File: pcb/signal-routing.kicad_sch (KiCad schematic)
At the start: 42 parts, among them U10 SN74LVC1G3157DCKR, U11 SN74HCS595PWR, U3 SN74LVC1G3157DCKR, U4 SN74LVC1G3157DCKR, U5 SN74LVC1G3157DCKR, U6 SN74LVC1G3157DCKR, U7 SN74LVC1G3157DCKR, U8 SN74LVC1G3157DCKR, U9 SN74LVC1G3157DCKR

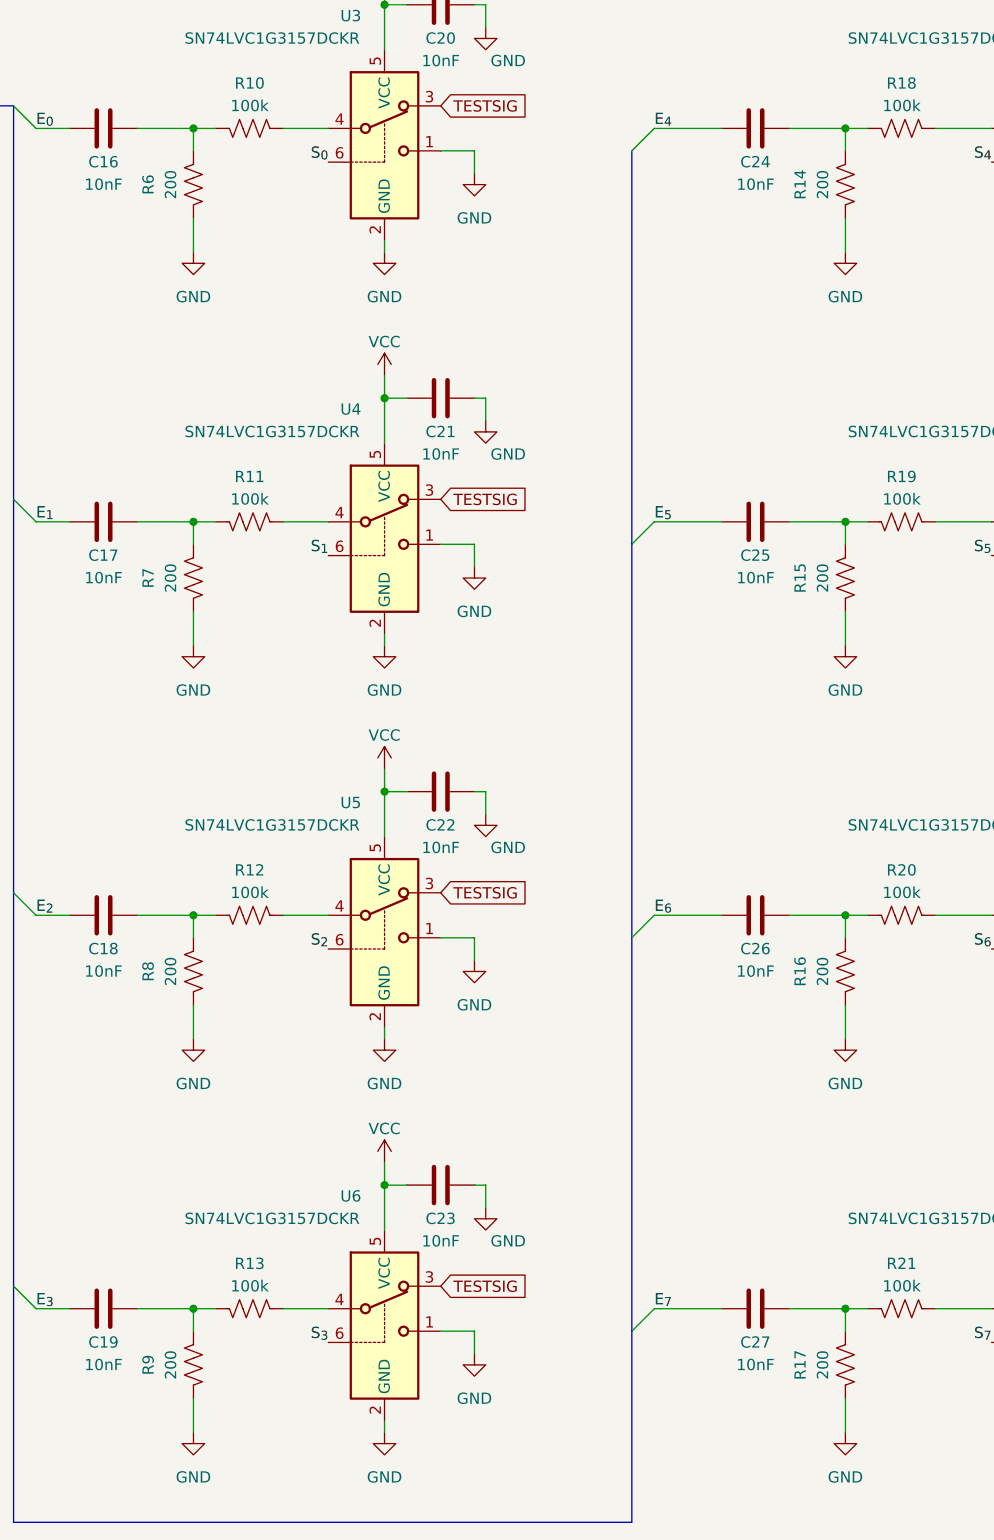
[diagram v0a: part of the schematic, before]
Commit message: Added OEPS PN.
Co-Authored-By: David Palma <78764277+davidpalma666@users.noreply.github.com>
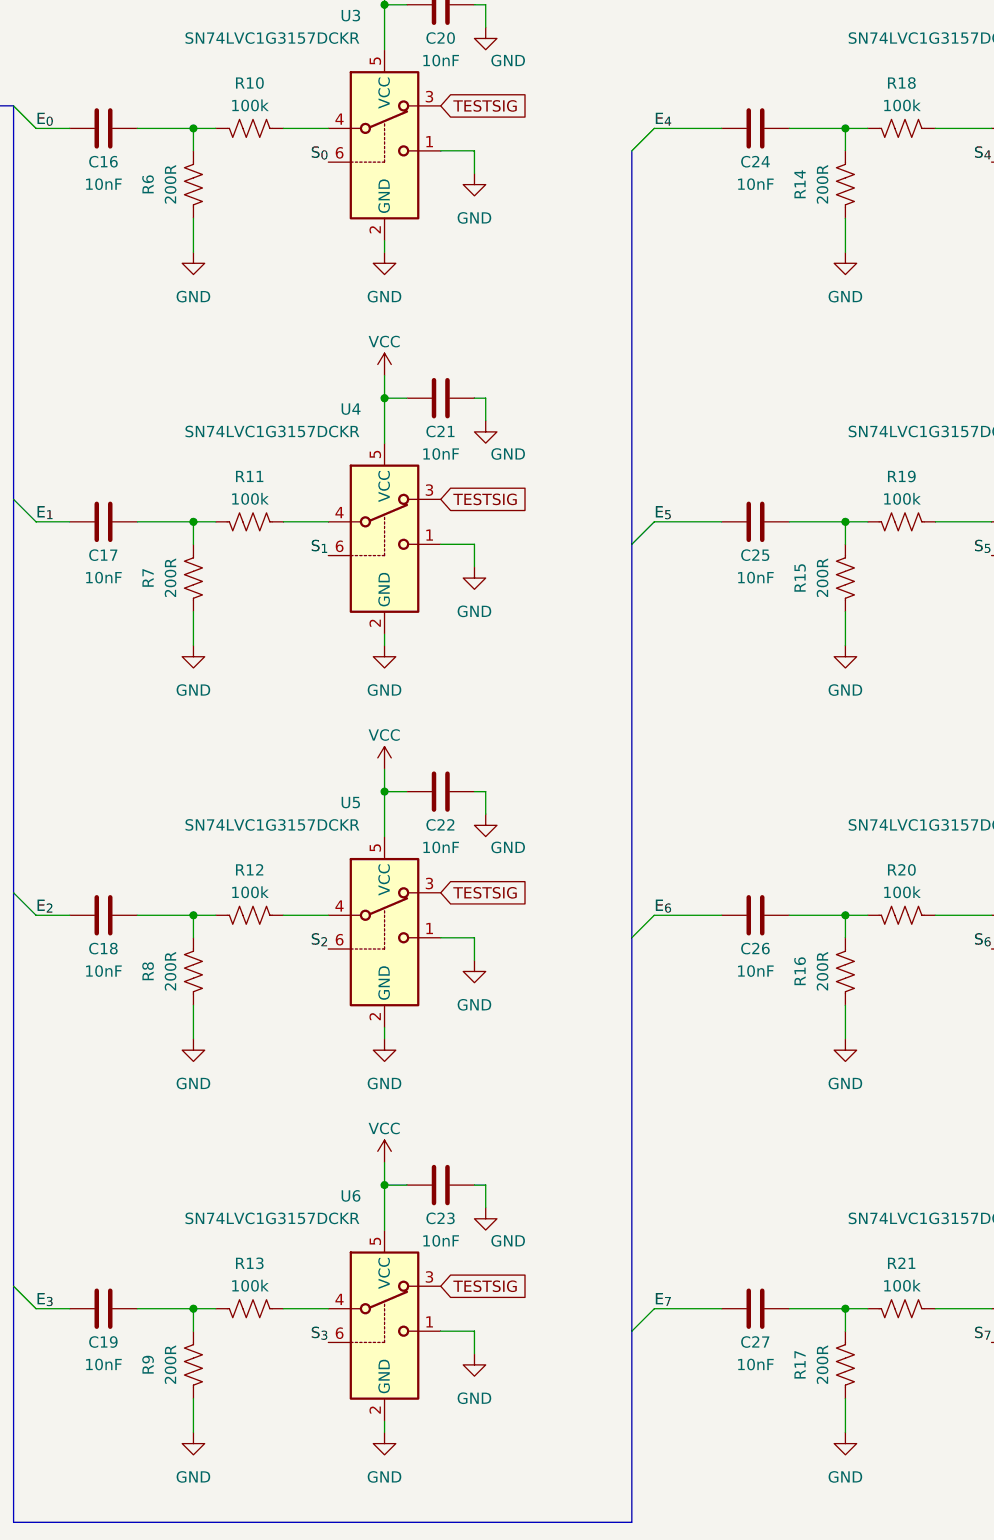
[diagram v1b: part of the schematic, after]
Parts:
- C16, C17, C18, C19, C20, C21, C22, C23, C24, C25, C26, C27, C28, C29, C30, C31: MPN (none) -> GRM155R71E103KA01D; OEPSPN (none) -> OEPS010067
- C32: MPN (none) -> C1005X7R1E104K050BB; OEPSPN (none) -> OEPS010050
- R10, R11, R12, R13, R18, R19, R20, R21: MPN (none) -> RG1005P-104-B-T5; OEPSPN (none) -> OEPS020175
- R14, R15, R16, R17, R6, R7, R8, R9: value 200 -> 200R; MPN (none) -> ERA-2AEB201X; OEPSPN (none) -> OEPS020171
- U10, U3, U4, U5, U6, U7, U8, U9: MPN (none) -> SN74LVC1G3157DCKR; OEPSPN (none) -> OEPS080161
- U11: MPN (none) -> SN74HCS595PWR; OEPSPN (none) -> OEPS080159

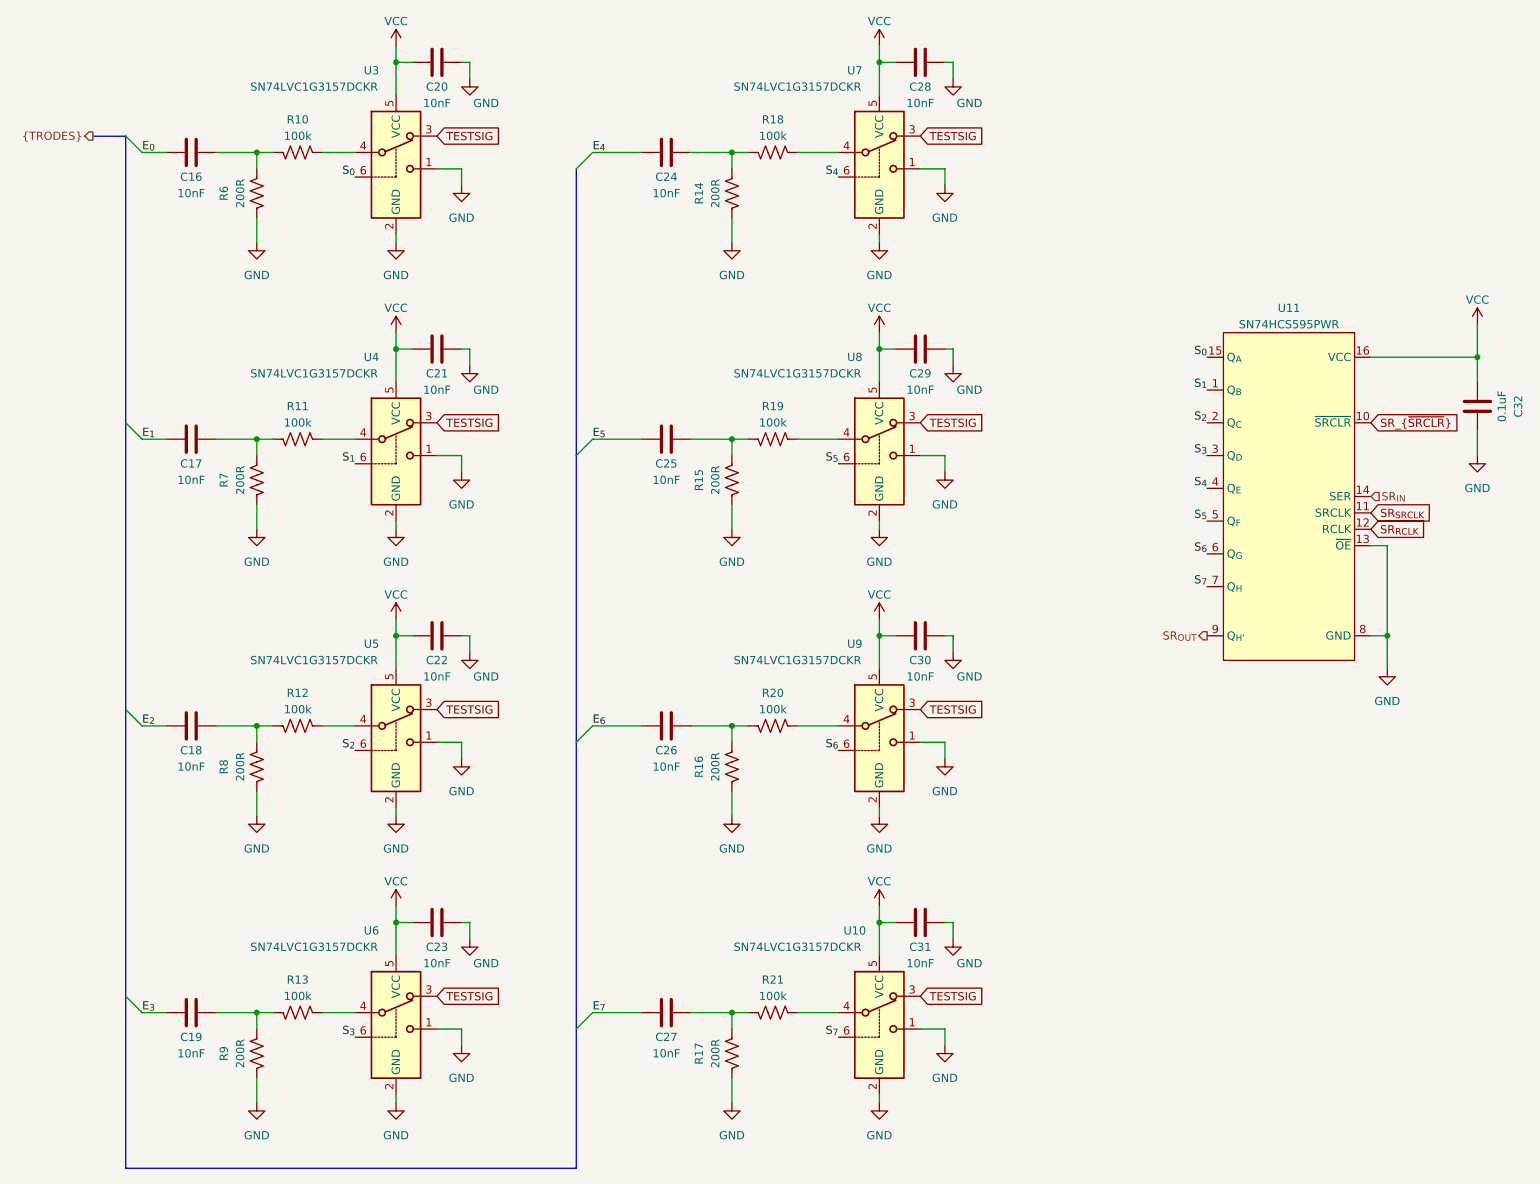
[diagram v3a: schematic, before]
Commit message: Use 1.25V reference voltage for electrode test signal
- This prevents large AC component when channel switch occurs.
- Previously the attenuator reference and nomimal electrode signals were
  both ground. Since the test signal is centered arround 1.25V, there
  the test signal is effectively a 1.25V square wave + the indented
  signal. The square waves edges were readily passed through the AC
  coupling capacitor.
- Add LCSC numbers to all required components for assembly.
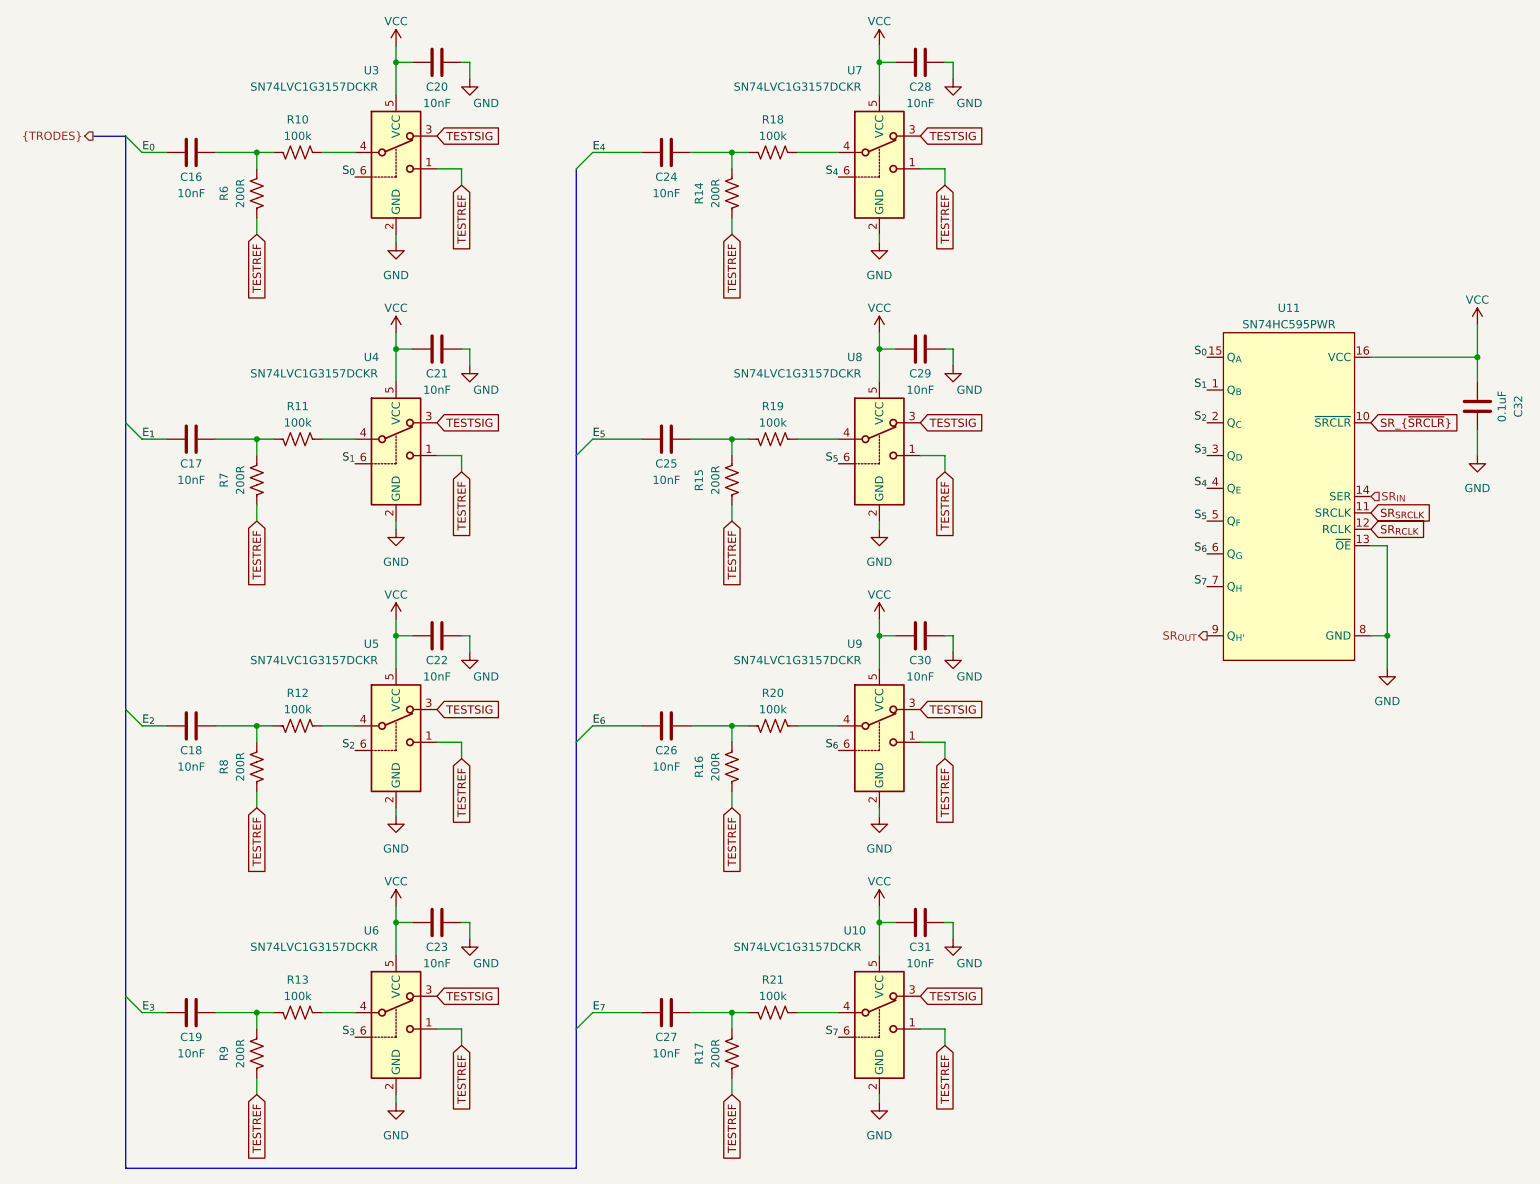
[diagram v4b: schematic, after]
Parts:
- C16, C17, C18, C19, C20, C21, C22, C23, C24, C25, C26, C27, C28, C29, C30, C31: LCSC (none) -> C60133; Voltage (none) -> 50V
- C32: LCSC (none) -> C105883; Voltage (none) -> 25V
- R10, R11, R12, R13, R18, R19, R20, R21: LCSC (none) -> C852472
- R14, R15, R16, R17, R6, R7, R8, R9: LCSC (none) -> C852625
- U10, U3, U4, U5, U6, U7, U8, U9: LCSC (none) -> C38663
- U11: value SN74HCS595PWR -> SN74HC595PWR; LCSC (none) -> C273642
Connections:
- net GND: no longer R14.2, R15.2, R16.2, R17.2, R6.2, R7.2, R8.2, R9.2, U10.1, U3.1, U4.1, U5.1, U6.1, U7.1, U8.1, U9.1
- new net TESTREF: R14.2, R15.2, R16.2, R17.2, R6.2, R7.2, R8.2, R9.2, U10.1, U3.1, U4.1, U5.1, U6.1, U7.1, U8.1, U9.1

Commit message: Implmenent bipolar test signal
- Generate internal negative rail
- Shift DAC output by VREF/2
- Replace analog switches with depletion mode switches to allow negative
  signals
- DC couple electrode inputs
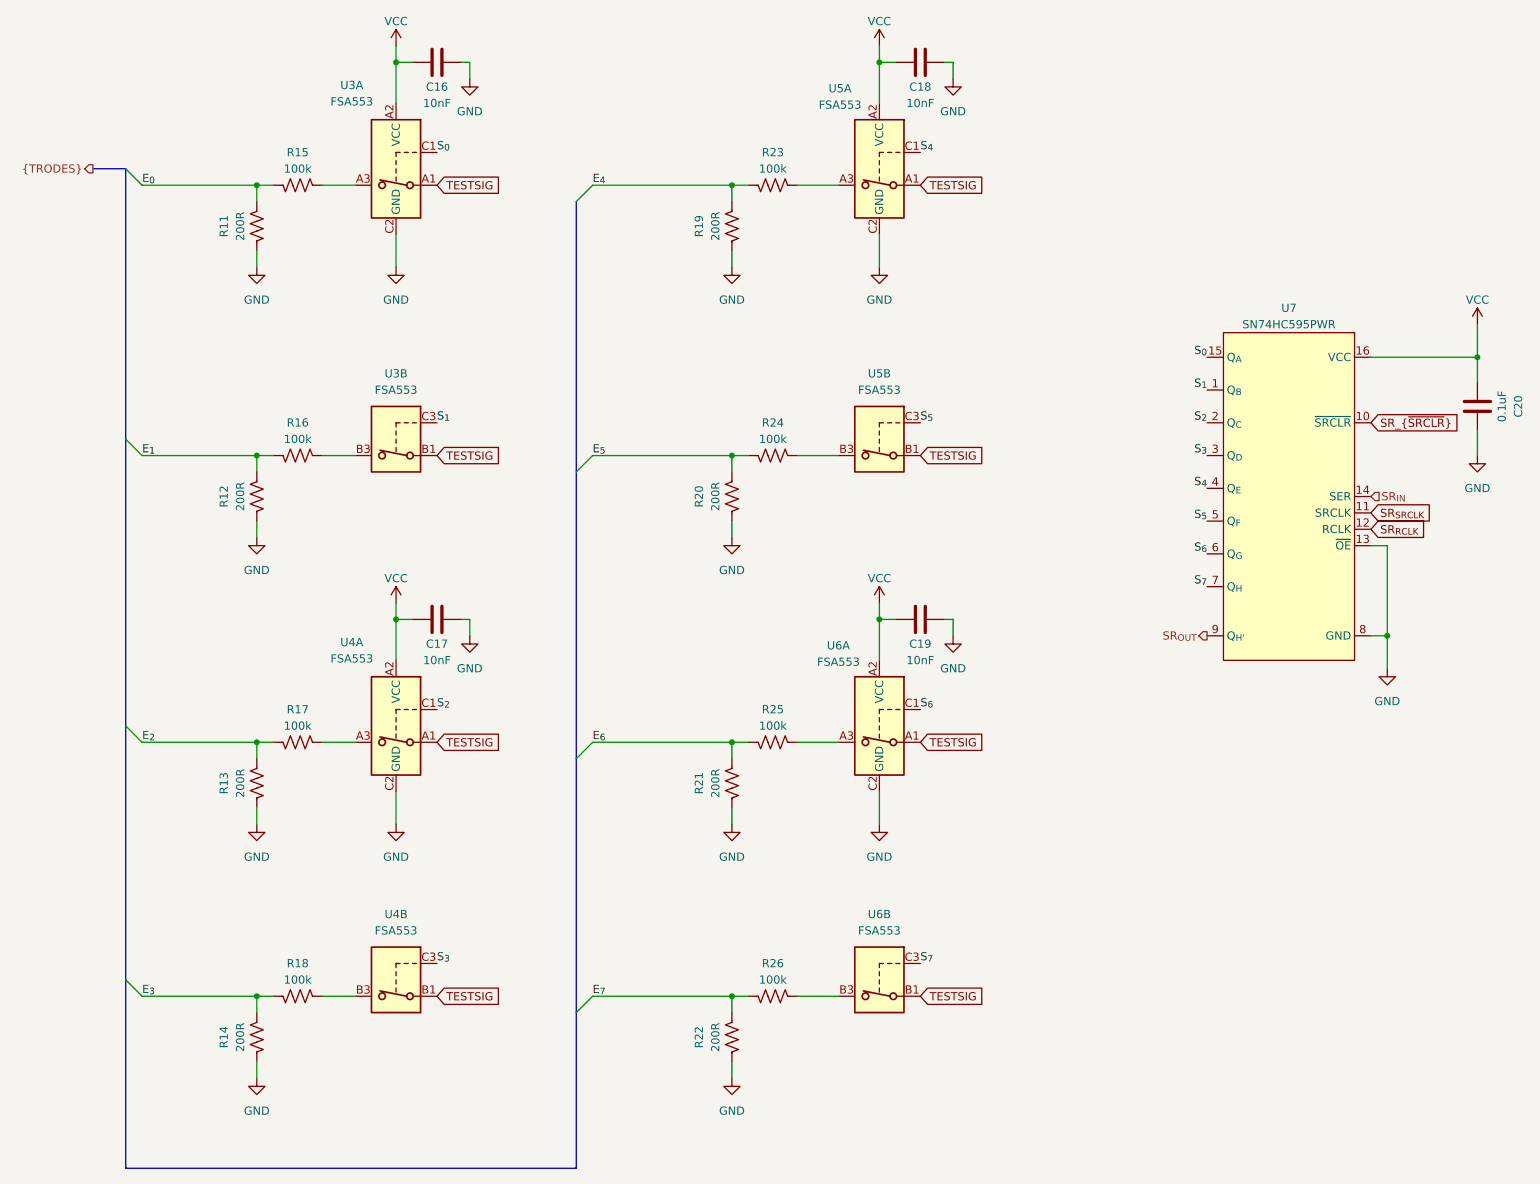
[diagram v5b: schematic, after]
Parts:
- removed C16, C17, C18, C19, C21, C23, C24, C25, C26, C27, C29, C31: 10nF, Capacitor_SMD:C_0402_1005Metric, symbol Device:C
- removed U10, U3, U4, U5, U6, U7, U8, U9: SN74LVC1G3157DCKR, Package_TO_SOT_SMD:SOT-363_SC-70-6, symbol open-ephys:SN74LVC1G3157DCKR
- added U3, U4, U5, U6: FSA553, open-ephys:ONSEMI_567SV_WLCSP9-3x3-1.215x1.385x0.581mm-P0.4mm, symbol open-ephys:FSA553
- renumbered C20 to C16, C22 to C17, C28 to C18, C30 to C19, C32 to C20, R6 to R11, R7 to R12, R8 to R13, R9 to R14, R10 to R15, R11 to R16, R12 to R17, R13 to R18, R14 to R19, R15 to R20, R16 to R21, R17 to R22, R18 to R23, R19 to R24, R20 to R25, R21 to R26, U11 to U7
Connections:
- net TESTREF is gone; now on net GND: R11.2, R12.2, R13.2, R14.2, R19.2, R20.2, R21.2, R22.2
- net E_{0}: now also R11.1, R15.2
- net E_{1}: now also R12.1, R16.2
- net E_{2}: now also R13.1, R17.2
- net E_{3}: now also R14.1, R18.2
- net E_{4}: now also R19.1, R23.2
- net E_{5}: now also R20.1, R24.2
- net E_{6}: now also R21.1, R25.2
- net E_{7}: now also R22.1, R26.2
- net GND: now also U3.C2 (GND), U4.C2 (GND), U5.C2 (GND), U6.C2 (GND)
- net S_{0}: now also U3.C1
- net S_{1}: now also U3.C3
- net S_{2}: now also U4.C1
- net S_{3}: now also U4.C3
- net S_{4}: now also U5.C1
- net S_{5}: now also U5.C3
- net S_{6}: now also U6.C1
- net S_{7}: now also U6.C3
- net TESTSIG: now also U3.A1, U3.B1, U4.A1, U4.B1, U5.A1, U5.B1, U6.A1, U6.B1
- net VCC: now also U3.A2 (VCC), U4.A2 (VCC), U5.A2 (VCC), U6.A2 (VCC)
- net at R26.1: now also U6.B3
- net at R25.1: now also U6.A3
- net at R16.1: now also U3.B3
- net at R15.1: now also U3.A3
- net at R18.1: now also U4.B3
- net at R17.1: now also U4.A3
- net at R23.1: now also U5.A3
- net at R24.1: now also U5.B3
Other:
- moved on the sheet: C17, C19, R11, R12, R13, R14, R15, R16, R17, R18, R19, R20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
